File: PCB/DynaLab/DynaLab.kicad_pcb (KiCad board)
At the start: 2 copper layers, 150 x 80 mm, 106 parts, among them J1 USB_C_Receptacle_USB2.0_16P, SW1 BOOT, SW2 REC/STOP, SW3 RESET, U1 LM393, U10 74AHCT125, U11 ITR8307-S17-TR8, U12 ITR8307-S17-TR8, U13 USBLC6-2SC6, U14 RP2040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

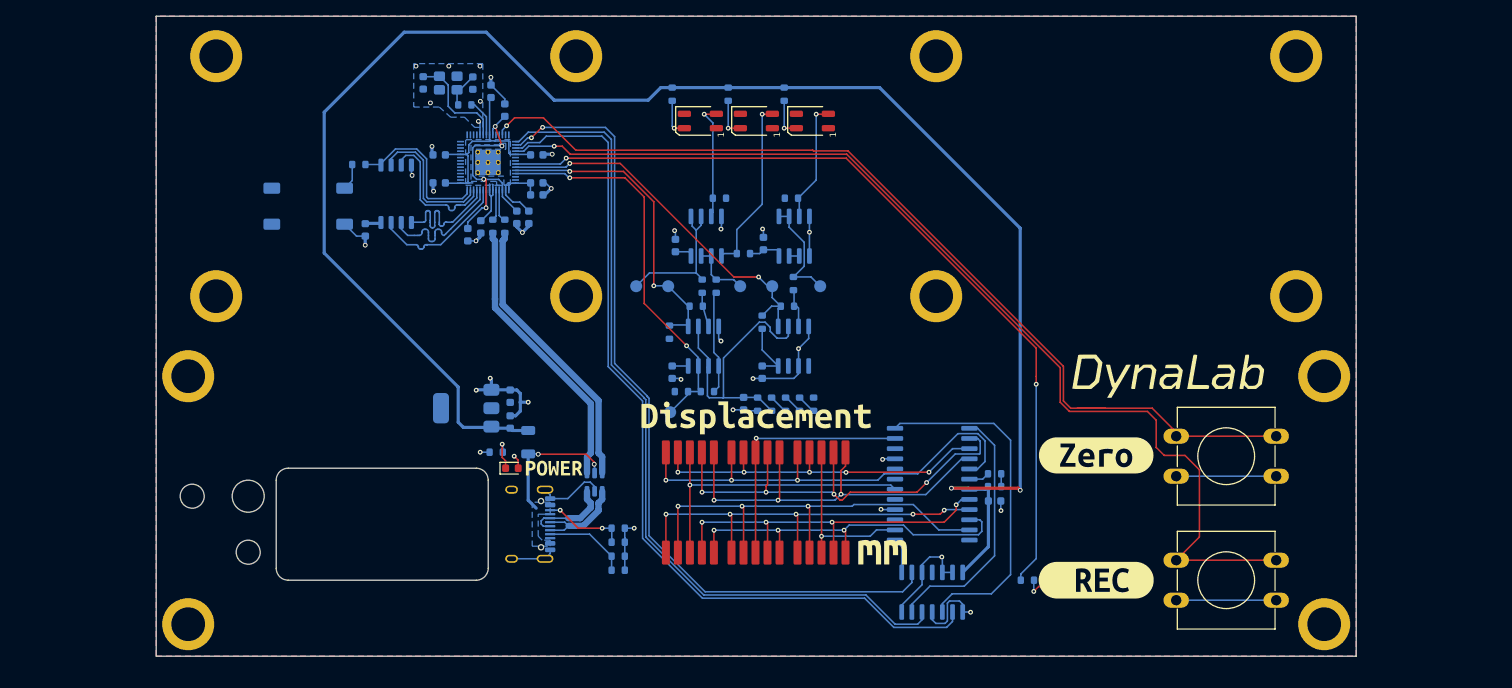
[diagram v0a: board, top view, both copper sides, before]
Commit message: atomise PCB projects for portability
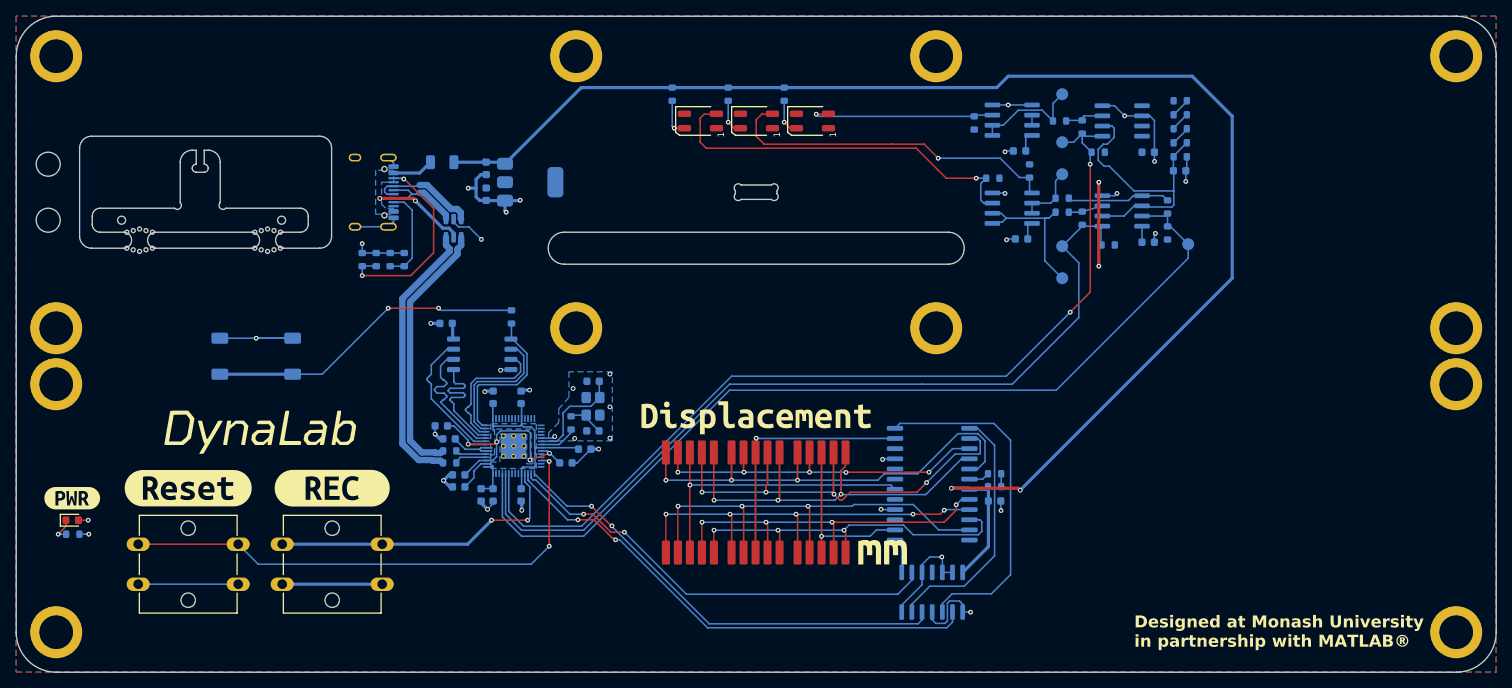
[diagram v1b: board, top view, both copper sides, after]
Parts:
- removed D1: REC, LED_SMD:LED_0603_1608Metric
- removed R26: 10k, Resistor_SMD:R_0603_1608Metric
- removed kibuzzard-6930ADF3: G***, kibuzzard-6930ADF3
- removed kibuzzard-6930BD82: G***, kibuzzard-6930BD82
- removed kibuzzard-6930BD9C: G***, kibuzzard-6930BD9C
- added kibuzzard-6964435B: G***, kibuzzard-6964435B, F.Cu at (253.8, 275.2)
- added kibuzzard-69644420: G***, kibuzzard-69644420, F.Cu at (286.2, 274.0)
- added kibuzzard-69645CED: G***, kibuzzard-69645CED, B.Cu at (421.7, 266.4)
- added kibuzzard-6964600A: G***, kibuzzard-6964600A, F.Cu at (268.2, 274.0)
- added mousebite1: VAL**, Footprints:mouse-bite-2mm-4mm, F.Cu at (262.2, 243.0)
- added mousebite2: VAL**, Footprints:mouse-bite-2mm-4mm, F.Cu at (278.2, 243.0)
- H1, H2, H3, H4, H5, H6, H7, H8: value SMTSO3030 -> SMTSO3060; footprint Footprints:MountingHole_SMTSO3030_3.2mm_M3 -> Footprints:MountingHole_SMTSO3060_3.2mm_M3
- H10, H11, H12, H9: value SMTSO3040 -> SMTSO3080; footprint Footprints:MountingHole_SMTSO3030_3.2mm_M3 -> Footprints:MountingHole_SMTSO3080_3.2mm_M3
- R30: value 10k -> 220
- SW2, SW3: footprint Button_Switch_THT:SW_PUSH-12mm -> Button_Switch_THT:SW_SPST_Omron_B3F-40xx
- moved SW3 130.5 mm to (262.0, 281.0)
- moved LOGO 113.7 mm to (277.1, 265.9)
- moved SW2 111.8 mm to (280.0, 281.0)
- moved TP4 68.1 mm to (393.2, 243.5), turned to 90 degrees
- moved R16 63.9 mm to (390.7, 242.1), turned to -90 degrees
- moved R13 62.0 mm to (390.7, 238.8), turned to -90 degrees
- moved C21 61.8 mm to (392.2, 234.3), turned to 0 degrees
- moved C1 61.7 mm to (388.2, 243.2), turned to 0 degrees
- moved R12 61.2 mm to (392.2, 232.6), turned to 0 degrees
- moved R7 60.6 mm to (392.2, 230.8), turned to 0 degrees
- moved R5 60.2 mm to (392.2, 229.1), turned to 0 degrees
- moved R4 59.8 mm to (392.2, 227.3), turned to 180 degrees
- moved R1 59.5 mm to (392.2, 225.6), turned to 180 degrees
- moved R10 55.9 mm to (383.2, 243.6), turned to 0 degrees
- moved C4 55.5 mm to (388.2, 232.0), turned to 0 degrees
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- renumbered G*** to LOGO
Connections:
- SW1 pad 1: GND -> /~{BOOT}
- SW1 pad 2: /~{BOOT} -> GND
- U14 pad 36: /LED_REC -> unconnected-(U14-GPIO24-Pad36)
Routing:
- net /LED_REC: track 105.0 -> 0.00 mm, vias 2 -> 0
- net /SW_REC: track 132.0 -> 37.6 mm, vias 1 -> 2
- net /PHOTO_C: track 47.1 -> 116.3 mm
- net /PHOTO_A: track 40.0 -> 107.1 mm, vias 2 -> 0
- net /PHOTO_B: track 49.7 -> 116.7 mm, vias 2 -> 0
- net /~{RESET}: track 120.8 -> 65.0 mm, vias 1 -> 2
- net /7SEG_CLK: track 104.6 -> 57.5 mm, vias 0 -> 2
- net /7SEG_DATA: track 102.9 -> 55.9 mm
- net /7SEG_~{CS}: track 108.6 -> 63.1 mm, vias 0 -> 2
- net /~{BOOT}: track 3.36 -> 40.0 mm, vias 0 -> 2
- net Net-(U2A-+): track 14.8 -> 47.5 mm
- net +5V: track 215.8 -> 187.7 mm
- net Net-(U2B-+): track 22.1 -> 42.8 mm
- net Net-(J1-CC2): track 10.4 -> 25.2 mm
- net Net-(U3A-+): track 15.3 -> 23.7 mm
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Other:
- board size 150 x 80 mm -> 185 x 82 mm
- board text added: "Break tabs"
- board text added: "Designed at Monash University in partnership with MATLAB®"
- board text added: "Inserts from this side"
- board text added: "MR"
- board text added: "Spring retaining post"

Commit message: add purchasing #s and some datasheets
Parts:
- moved C1 257.8 mm to (180.8, 90.2)
- moved C10 257.8 mm to (102.4, 121.8)
- moved C11 257.8 mm to (110.3, 116.1)
- moved C12 257.8 mm to (102.4, 109.6)
- moved C13 257.8 mm to (98.9, 109.6)
- moved C14 257.8 mm to (108.0, 117.8)
- moved C15 257.8 mm to (98.9, 121.8)
- moved C16 257.8 mm to (93.0, 100.4)
- moved C17 257.8 mm to (111.4, 107.6)
- moved C18 257.8 mm to (111.3, 113.8)
- moved C19 257.8 mm to (98.0, 81.0)
- moved C2 257.8 mm to (164.9, 89.8)
- moved C20 257.8 mm to (98.0, 84.2)
- moved C21 257.8 mm to (184.7, 81.3)
- moved C22 257.8 mm to (161.6, 122.6)
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
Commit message: repo and library maintenance
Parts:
- removed the G*** at (214.2, 123.5)
- removed LOGO: LOGO, LOGO
- removed kibuzzard-69310248: G***, kibuzzard-69310248
- removed kibuzzard-69644420: G***, kibuzzard-69644420
- removed kibuzzard-6964600A: G***, kibuzzard-6964600A
- added G***: LOGO, LOGO, F.Cu at (169.5, 130.5)
- added G***: LOGO, LOGO, F.Cu at (189.4, 125.7)
- added G***: LOGO, LOGO, B.Cu at (197.2, 123.0)
- added REF**: OSHW-Logo2_9.8x8mm_SilkScreen_noText, Footprints:OSHW-Logo2_9.8x8mm_SilkScreen_noText, F.Cu at (169.7, 140.5)
- added kibuzzard-6978203B: G***, kibuzzard-6978203B, B.Cu at (197.2, 132.7)
- added kibuzzard-6978204E: G***, kibuzzard-6978204E, B.Cu at (197.3, 134.5)
- added kibuzzard-6978363D: G***, kibuzzard-6978363D, F.Cu at (195.3, 127.1)
- added kibuzzard-69783696: G***, kibuzzard-69783696, F.Cu at (195.3, 131.6)
- added kibuzzard-697836DA: G***, kibuzzard-697836DA, F.Cu at (218.8, 134.0)
- added kibuzzard-6978422B: G***, kibuzzard-6978422B, F.Cu at (80.8, 121.0)
- added kibuzzard-69784254: G***, kibuzzard-69784254, F.Cu at (60.8, 121.0)
- added kibuzzard-697848C9: G***, kibuzzard-697848C9, F.Cu at (169.5, 124.0)
- C1, C2, C21, C22, C3, C4: value 100n -> 100nF
- mousebite1, mousebite2: footprint Footprints:mouse-bite-2mm-4mm -> Footprints:mouse-bite-2mm-4mm-single-sided
- moved kibuzzard-69310180 16.9 mm to (197.2, 115.0)
- moved kibuzzard-69310240 16.9 mm to (197.2, 130.7)
- moved kibuzzard-69645CED 16.9 mm to (197.2, 112.9)
- moved SW2 2.00 mm to (74.5, 128.0)
- moved mousebite1 0.20 mm to (54.7, 90.2), turned to 180 degrees
- moved mousebite2 0.20 mm to (70.7, 90.2), turned to 180 degrees
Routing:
- net GND: track 146.6 -> 144.8 mm
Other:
- outline, holes or cut-outs redrawn
- board text added: "Design by Michael Ruppe 2026"
- board text added: "Designed at Monash University in partnership with MathWorks®"
- board text removed: "Designed at Monash University in partnership with MATLAB®"
